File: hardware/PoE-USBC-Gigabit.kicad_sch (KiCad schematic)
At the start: 0 parts

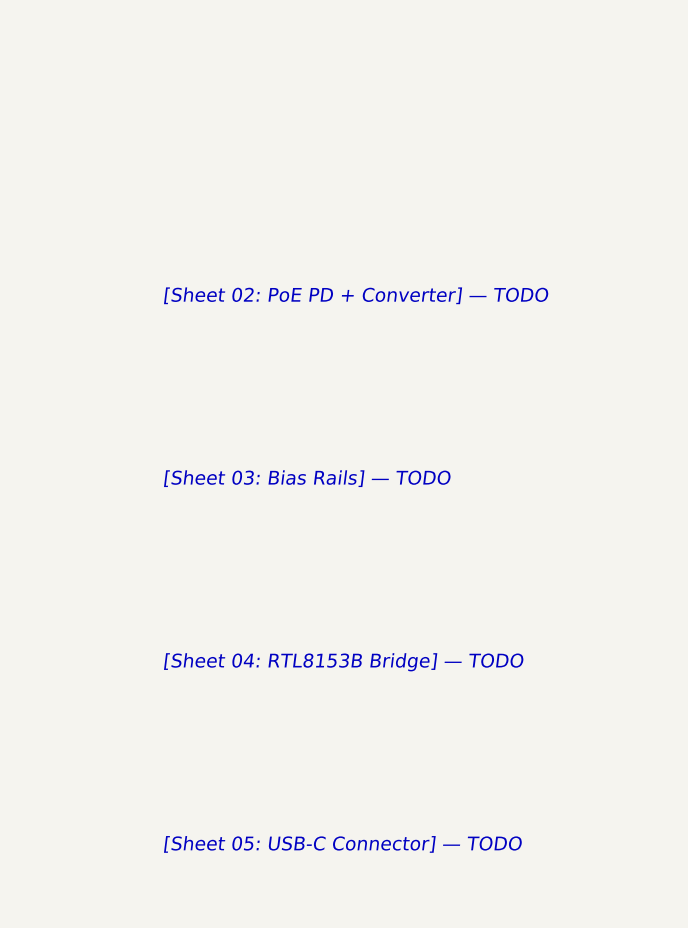
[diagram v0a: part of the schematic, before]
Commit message: Add Sheet 02 starter (PoE PD + Flyback Converter) + build guide
- hardware/02_PoE_PD_Converter.kicad_sch: sub-sheet with all 6
  hierarchical labels (PAIR_A/B HI/LO inputs, +5V and GND outputs),
  annotated placement blocks for primary and secondary sides,
  isolation barrier marker, Si3402-B pin guide, feedback notes
- hardware/PoE-USBC-Gigabit.kicad_sch: root sheet now references
  02_PoE_PD_Converter with matching hierarchical pins (page 3)
- docs/BUILD-SHEET-02.md: 12-step build guide covering bridge rectifiers,
  Si3402-B wiring, transformer polarity, Y-cap isolation, TL431+PC817B
  feedback network, snubber, ERC checklist, and common gotchas
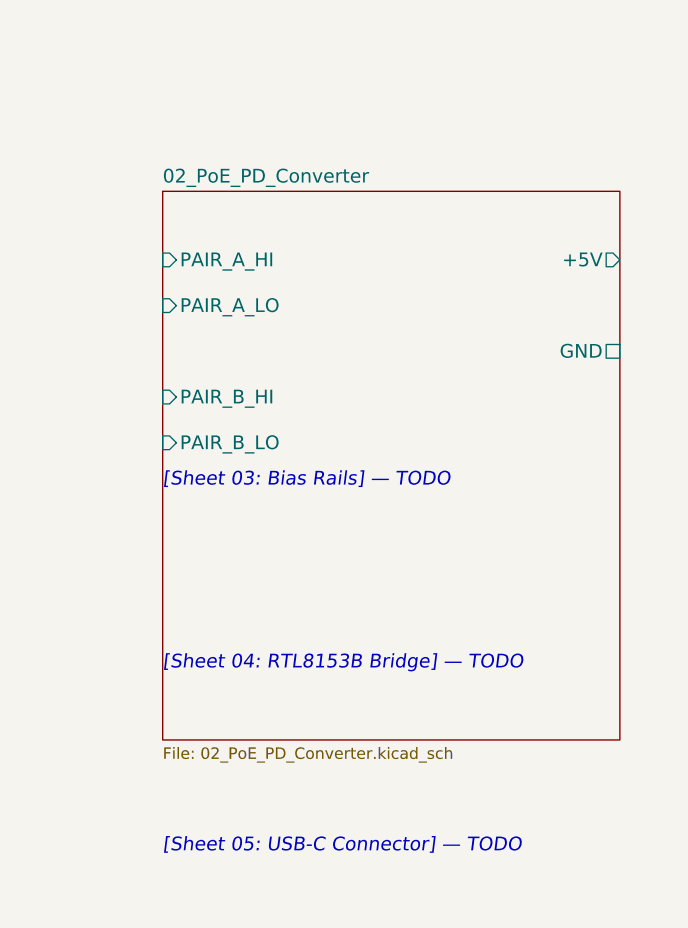
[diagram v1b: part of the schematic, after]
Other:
- added sheet 02_PoE_PD_Converter (02_PoE_PD_Converter.kicad_sch)
- note removed: "[Sheet 02: PoE PD + Converter] — TODO"
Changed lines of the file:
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@@
 		)
 	)
-	(text "[Sheet 02: PoE PD + Converter] — TODO"
+	(sheet
+		(at 109.22 38.1)
+		(size 50.8 60.96)
 		(exclude_from_sim no)
-		(at 109.22 50.8 0)
-		(effects (font (size 1.524 1.524) italic) (justify left bottom))
+		(in_bom yes)
+		(on_board yes)
+		(dnp no)
+		(fields_autoplaced yes)
+		(stroke (width 0.1524) (type solid))
+		(fill (color 0 0 0 0.0000))
+		(property "Sheetname" "02_PoE_PD_Converter"
+			(at 109.22 37.3104 0)
+			(effects (font (size 1.524 1.524)) (justify left bottom))
+		)
+		(property "Sheetfile" "02_PoE_PD_Converter.kicad_sch"
+			(at 109.22 99.8314 0)
+			(effects (font (size 1.27 1.27)) (justify left top))
+		)
+		(pin "PAIR_A_HI" input (at 109.22 45.72 180)
+			(effects (font (size 1.524 1.524)) (justify left))
+		)
+		(pin "PAIR_A_LO" input (at 109.22 50.8 180)
+			(effects (font (size 1.524 1.524)) (justify left))
+		)
+		(pin "PAIR_B_HI" input (at 109.22 60.96 180)
+			(effects (font (size 1.524 1.524)) (justify left))
+		)
+		(pin "PAIR_B_LO" input (at 109.22 66.04 180)
+			(effects (font (size 1.524 1.524)) (justify left))
+		)
+		(pin "+5V" output (at 160.02 45.72 0)
+			(effects (font (size 1.524 1.524)) (justify right))
+		)
+		(pin "GND" passive (at 160.02 55.88 0)
+			(effects (font (size 1.524 1.524)) (justify right))
+		)
+		(instances
+			(project "PoE-USBC-Gigabit"
+				(path "/00000000-0000-0000-0000-000000000001"
+					(page "3")
+				)
+			)
+		)
 	)
 	(text "[Sheet 03: Bias Rails] — TODO"
